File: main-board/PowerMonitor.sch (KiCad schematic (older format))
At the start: 0 parts

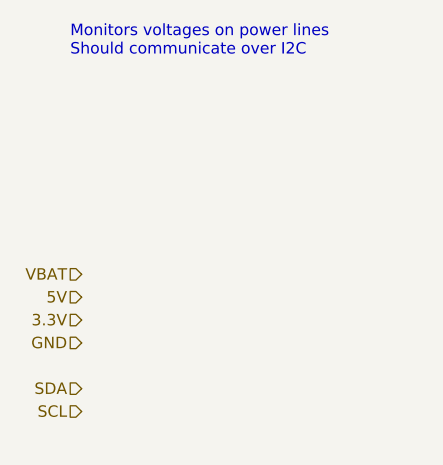
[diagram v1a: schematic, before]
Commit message: Even more subsheets
switched monitor and temp sensors to ADC. added temp sensors
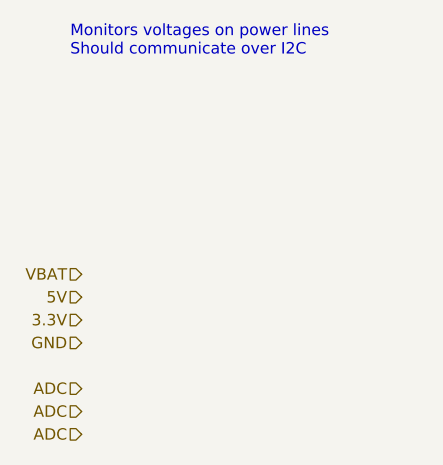
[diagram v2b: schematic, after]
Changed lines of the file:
@@
 $Descr A4 11693 8268
 encoding utf-8
-Sheet 20 23
+Sheet 19 23
 Title ""
 Date ""
@@
 Comment4 ""
 $EndDescr
-Text HLabel 3000 4000 0    50   Input ~ 0
-SDA
-Text HLabel 3000 4100 0    50   Input ~ 0
-SCL
 Text HLabel 3000 3700 0    50   Input ~ 0
 3.3V
@@
 Text Notes 2950 2550 0    50   ~ 0
 Monitors voltages on power lines\nShould communicate over I2C
+Text HLabel 3000 4000 0    50   Input ~ 0
+ADC
+Text HLabel 3000 4100 0    50   Input ~ 0
+ADC
+Text HLabel 3000 4200 0    50   Input ~ 0
+ADC
 $EndSCHEMATC
